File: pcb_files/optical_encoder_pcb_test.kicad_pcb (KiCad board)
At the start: 2 copper layers, 52.5 x 55 mm, 31 parts, among them J1 Conn_01x01_Pin, J10 Conn_DF13_malex06, J11 Conn_DF13_malex05, J12 Conn_DF13_malex05, J13 Conn_THT_padx04, J14 Conn_THT_padx04, J2 Conn_01x02_Pin, J3 Conn_01x04_Pin, J4 Conn_01x03_Pin, J5 Conn_01x04_Pin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

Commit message: Propositions de corrections v2.
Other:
- board text added: "C1 & C2 sont à placer au plus près de la pin 14"
- board text added: "Même chose avec C3, C4 & C5"
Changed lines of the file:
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@@
 		)
 		(property "Value" "Conn_THT_padx04"
-			(at 0 9.95 270)
+			(at 0 9.95 -90)
 			(layer "F.Fab")
 			(hide yes)
@@
 		)
 		(fp_text user "${REFERENCE}"
-			(at 0 3.81 360)
+			(at 0 3.81 0)
 			(layer "F.Fab")
 			(effects
@@
 		)
 	)
+	(gr_text "C1 & C2 sont à placer au plus près de la pin 14"
+		(at 109 76.3 0)
+		(layer "Cmts.User")
+		(effects
+			(font
+				(size 1.5 1.5)
+				(thickness 0.3)
+				(bold yes)
+			)
+			(justify left bottom)
+		)
+	)
+	(gr_text "Même chose avec C3, C4 & C5"
+		(at 109 80 0)
+		(layer "Cmts.User")
+		(effects
+			(font
+				(size 1.5 1.5)
+				(thickness 0.3)
+				(bold yes)
+			)
+			(justify left bottom)
+		)
+	)

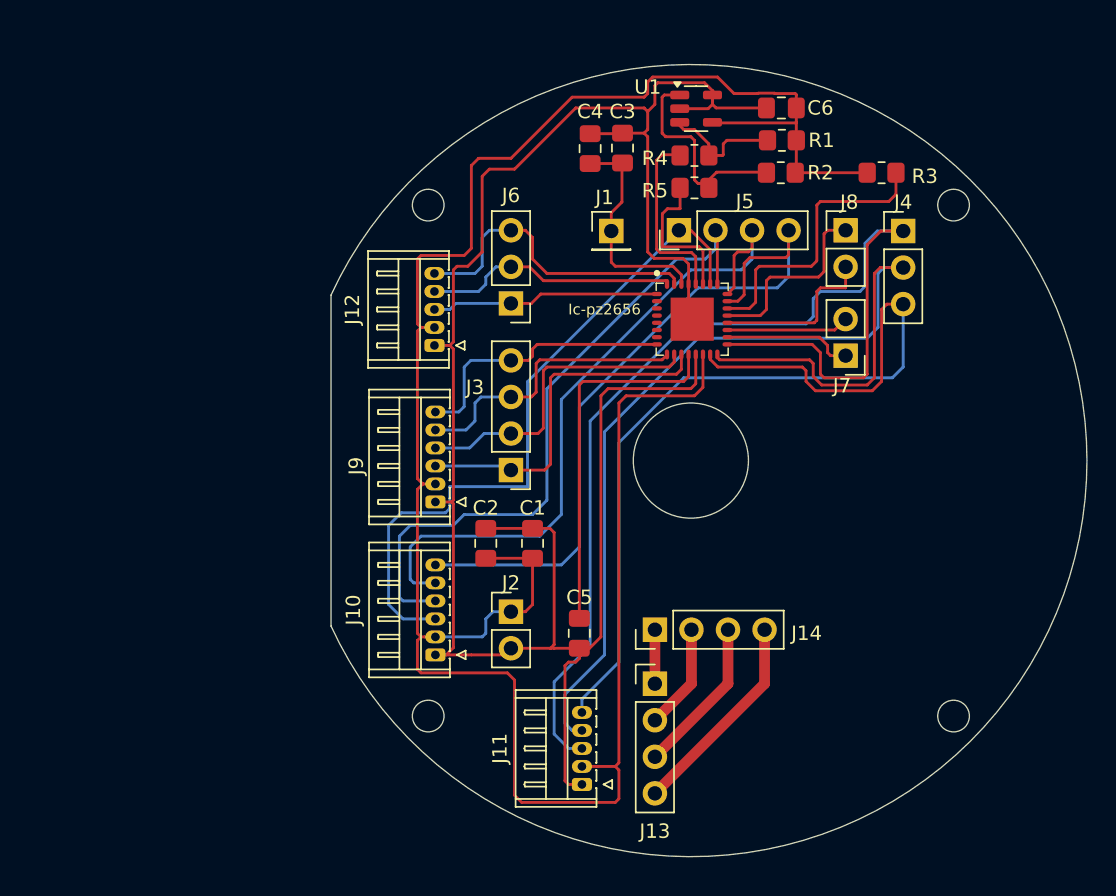
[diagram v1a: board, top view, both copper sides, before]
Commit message: Story 2 : add voltage regulator, fix configuration, modify connectors
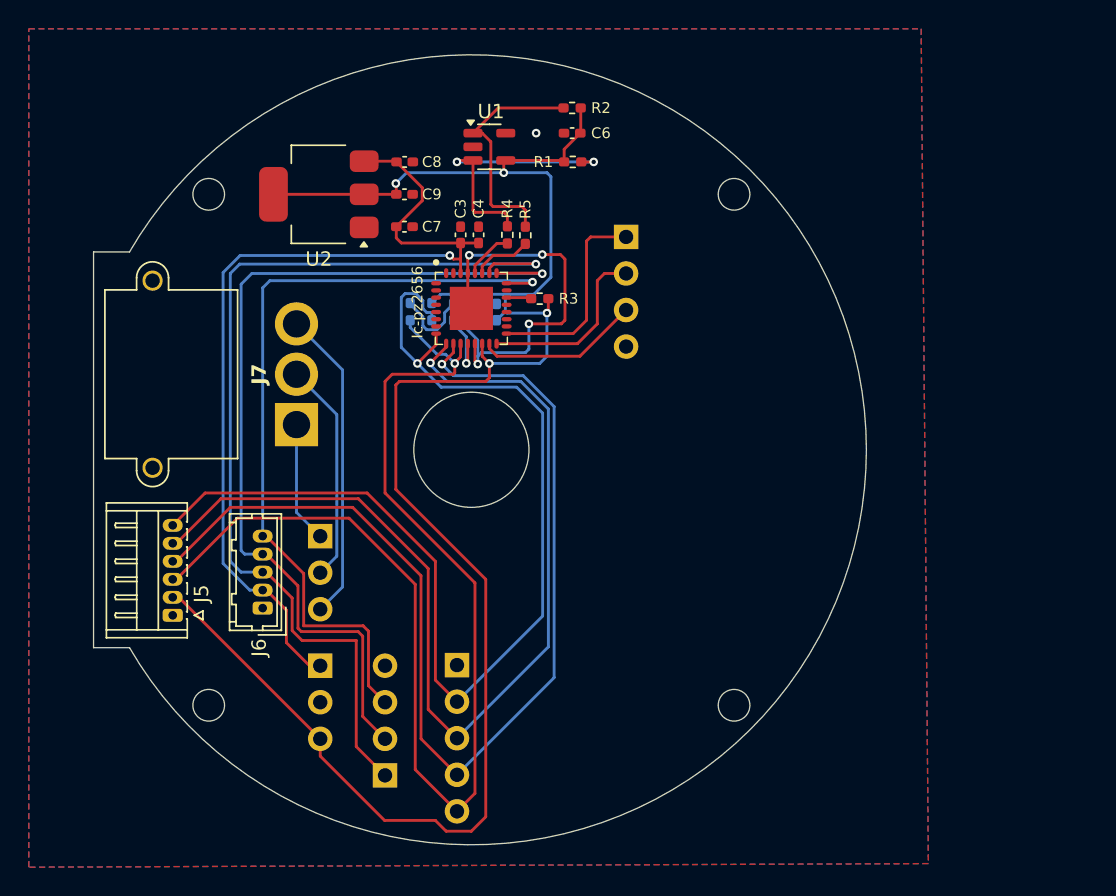
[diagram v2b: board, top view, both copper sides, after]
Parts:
- removed J10, J9: Conn_DF13_malex06, Connector_Hirose:Hirose_DF13-06P-1.25DS_1x06_P1.25mm_Horizontal
- removed J11, J12: Conn_DF13_malex05, Connector_Hirose:Hirose_DF13-05P-1.25DS_1x05_P1.25mm_Horizontal
- removed J13, J14: Conn_THT_padx04, Connector_PinHeader_2.54mm:PinHeader_1x04_P2.54mm_Vertical
- added C7: 1uF, Capacitor_SMD:C_0402_1005Metric_Pad0.74x0.62mm_HandSolder, F.Cu at (115.8, 107.0)
- added C8: 100nF, Capacitor_SMD:C_0402_1005Metric_Pad0.74x0.62mm_HandSolder, F.Cu at (115.9, 102.5)
- added C9: 10uF, Capacitor_SMD:C_0402_1005Metric_Pad0.74x0.62mm_HandSolder, F.Cu at (115.8, 104.8)
- added R6: 10K, Resistor_SMD:R_0402_1005Metric_Pad0.72x0.64mm_HandSolder, B.Cu at (116.2, 112.9)
- added R7: 10K, Resistor_SMD:R_0402_1005Metric_Pad0.72x0.64mm_HandSolder, B.Cu at (117.8, 112.9)
- added U2: AMS1117-3.3, Package_TO_SOT_SMD:SOT-223-3_TabPin2, F.Cu at (109.9, 104.8)
- C1, C2, C5: footprint Capacitor_SMD:C_0805_2012Metric_Pad1.18x1.45mm_HandSolder -> Capacitor_SMD:C_0402_1005Metric_Pad0.74x0.62mm_HandSolder; moved to B.Cu
- C3, C4, C6: footprint Capacitor_SMD:C_0805_2012Metric_Pad1.18x1.45mm_HandSolder -> Capacitor_SMD:C_0402_1005Metric_Pad0.74x0.62mm_HandSolder
- J1: value Conn_01x01_Pin -> Conn_01x03_Pin; footprint Connector_PinHeader_2.54mm:PinHeader_1x01_P2.54mm_Vertical -> Connector_PinHeader_2.54mm:PinHeader_1x03_P2.54mm_Vertical; moved to B.Cu
- J2: value Conn_01x02_Pin -> Conn_01x05_Pin; footprint Connector_PinHeader_2.54mm:PinHeader_1x02_P2.54mm_Vertical -> Connector_PinHeader_2.54mm:PinHeader_1x05_P2.54mm_Vertical; moved to B.Cu
- J3: moved to B.Cu
- J4: value Conn_01x03_Pin -> Conn_01x04_Pin; footprint Connector_PinHeader_2.54mm:PinHeader_1x03_P2.54mm_Vertical -> Connector_PinHeader_2.54mm:PinHeader_1x04_P2.54mm_Vertical; moved to B.Cu
- J5: value Conn_01x04_Pin -> Conn_DF13_male_01x06; footprint Connector_PinHeader_2.54mm:PinHeader_1x04_P2.54mm_Vertical -> Connector_Hirose:Hirose_DF13-06P-1.25DS_1x06_P1.25mm_Horizontal
- J6: value Conn_01x03_Pin -> Conn_DF13_male_01x05; footprint Connector_PinHeader_2.54mm:PinHeader_1x03_P2.54mm_Vertical -> Connector_Hirose:Hirose_DF13-05P-1.25DSA_1x05_P1.25mm_Vertical
- J7: value Conn_01x02_Pin -> Conn_AMASS_male_01x03; footprint Connector_PinHeader_2.54mm:PinHeader_1x02_P2.54mm_Vertical -> Connector_AMASS:AMASS_MR30PW-M_1x03_P3.50mm_Horizontal
- J8: value Conn_01x02_Pin -> Conn_01x03_Pin; footprint Connector_PinHeader_2.54mm:PinHeader_1x02_P2.54mm_Vertical -> Connector_PinHeader_2.54mm:PinHeader_1x03_P2.54mm_Vertical; moved to B.Cu
- R1, R2, R3, R4, R5: footprint Resistor_SMD:R_0805_2012Metric_Pad1.20x1.40mm_HandSolder -> Resistor_SMD:R_0402_1005Metric_Pad0.72x0.64mm_HandSolder
- moved J4 52.2 mm to (114.5, 145.1)
- moved J5 44.2 mm to (99.8, 134.0)
- moved J8 42.2 mm to (110.0, 128.5), turned to 180 degrees
- moved J7 38.4 mm to (108.3, 120.8), turned to 90 degrees
- moved J1 36.3 mm to (110.0, 137.5), turned to 180 degrees
- moved J6 27.3 mm to (106.0, 133.5), turned to 90 degrees
- moved R3 25.3 mm to (125.2, 112.0), turned to 180 degrees
- moved C5 24.0 mm to (119.2, 112.9), turned to -90 degrees
- moved J3 18.1 mm to (131.2, 107.7)
- moved C1 16.3 mm to (122.2, 112.9)
- moved C2 16.1 mm to (120.8, 112.9)
- moved Ic-pz2656 15.4 mm to (120.5, 112.7)
- moved REF** 15.3 mm to (138.8, 104.8)
- moved REF** 15.3 mm to (102.2, 140.2)
- moved REF** 15.3 mm to (102.2, 104.8)
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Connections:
- C1 pad 2: VDDIO -> +3.3V
- C2 pad 2: VDDIO -> +3.3V
- C3 pad 2: VDDA -> +5V
- C4 pad 2: VDDA -> +5V
- C6 pad 2: VDDIO -> +3.3V
- Ic-pz2656 pad 1: /CFG0 -> GND
- Ic-pz2656 pad 10: /PA1 -> /SPI_MOSI
- Ic-pz2656 pad 11: /PA0 -> /SPI_MISO
- Ic-pz2656 pad 14: VDDIO -> +3.3V
- Ic-pz2656 pad 15: /PB2 -> /BiSS_MA
- Ic-pz2656 pad 16: /PB1 -> /BiSS_SLI
- Ic-pz2656 pad 17: /PB0 -> /BiSS_SLO
- Ic-pz2656 pad 18: /ACL -> unconnected-(Ic-pz2656-ACL-Pad18)
- Ic-pz2656 pad 19: /ADA -> unconnected-(Ic-pz2656-ADA-Pad19)
- Ic-pz2656 pad 20: /ERR_IN -> unconnected-(Ic-pz2656-GPIO(1)-Pad20)
- Ic-pz2656 pad 21: /RDY -> unconnected-(Ic-pz2656-GPIO(0)-Pad21)
- Ic-pz2656 pad 23: /PC3 -> unconnected-(Ic-pz2656-PORTC(3)-Pad23)
- Ic-pz2656 pad 24: /PC2 -> /A
- Ic-pz2656 pad 25: /PC1 -> /B
- Ic-pz2656 pad 26: /PC0 -> /Z
- Ic-pz2656 pad 30: VDDA -> +5V
- Ic-pz2656 pad 31: /CFG2 -> GND
- Ic-pz2656 pad 32: /CFG1 -> GND
- Ic-pz2656 pad 8: /PA3 -> /SPI_~{CS}
- Ic-pz2656 pad 9: /PA2 -> /SPI_SCLK
- J1 pad 1: VDDA -> +5V
- J2 pad 1: VDDIO -> GND
- J2 pad 2: GND -> /SPI_~{CS}
- J3 pad 1: /PA0 -> /BiSS_SLO
- J3 pad 2: /PA1 -> /BiSS_SLI
- J3 pad 3: /PA2 -> /BiSS_MA
- J3 pad 4: /PA3 -> GND
- J4 pad 1: /PB0 -> /Z
- J4 pad 2: /PB1 -> /B
- J4 pad 3: /PB2 -> /A
- J5 pad 1: /PC0 -> GND
- J5 pad 2: /PC1 -> +3.3V
- J5 pad 3: /PC2 -> /SPI_MISO
- J5 pad 4: /PC3 -> /SPI_MOSI
- J6 pad 1: /CFG0 -> GND
- J6 pad 2: /CFG1 -> +5V
- J6 pad 3: /CFG2 -> /Z
- J7 pad 1: /ACL -> /P1
- J7 pad 2: /ADA -> /P2
- J8 pad 1: /RDY -> /P1
- J8 pad 2: /ERR_IN -> /P2
- R1 pad 2: VDDIO -> +3.3V
- R2 pad 2: VDDIO -> +3.3V
- R3 pad 1: VDDIO -> +3.3V
- U1 pad 4: VDDIO -> +3.3V
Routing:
- net VDDIO: track 159.0 -> 0.00 mm
- net +3.3V: track 0.00 -> 132.0 mm, vias 0 -> 4
- net GND: track 148.1 -> 37.4 mm, vias 0 -> 5
- net /SPI_MISO: track 0.00 -> 82.4 mm, vias 0 -> 1
- net /PB0: track 78.2 -> 0.00 mm
- net /SPI_~{CS}: track 0.00 -> 75.5 mm, vias 0 -> 1
- net /SPI_MOSI: track 0.00 -> 74.8 mm, vias 0 -> 1
- net /PB1: track 72.5 -> 0.00 mm
- net /SPI_SCLK: track 0.00 -> 70.6 mm, vias 0 -> 1
- net /Z: track 0.00 -> 67.8 mm, vias 0 -> 1
- net /PB2: track 66.6 -> 0.00 mm
- net +5V: track 0.00 -> 65.3 mm, vias 0 -> 1
- net /B: track 0.00 -> 63.3 mm, vias 0 -> 1
- net /A: track 0.00 -> 55.7 mm, vias 0 -> 1
- net /PC3: track 50.3 -> 0.00 mm
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- added copper zone on B.Cu, net GND
- added copper zone on F.Cu, net GND
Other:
- board size 52.5 x 55 mm -> 53.7 x 54.9 mm
- board text removed: "C1 & C2 sont à placer au plus près de la pin 14"
- board text removed: "Même chose avec C3, C4 & C5"
